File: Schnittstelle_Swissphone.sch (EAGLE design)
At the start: 22 parts, among them IC1 FT232RL, IC2 LM317LD

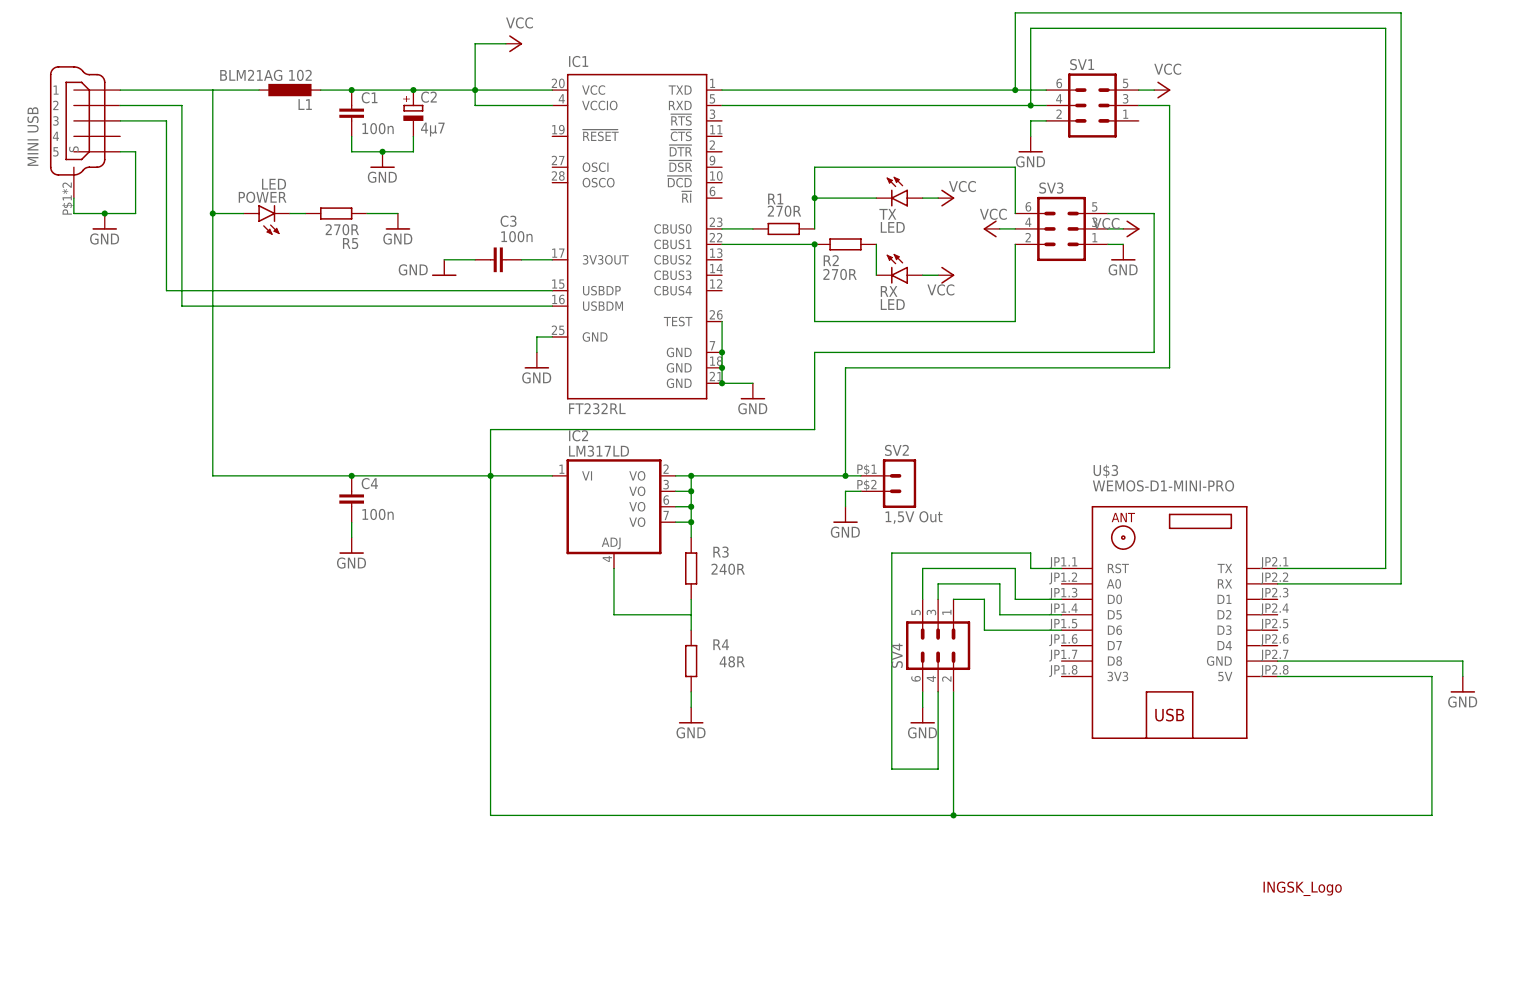
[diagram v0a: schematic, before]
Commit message: add Arduino Nano and ENC28J60
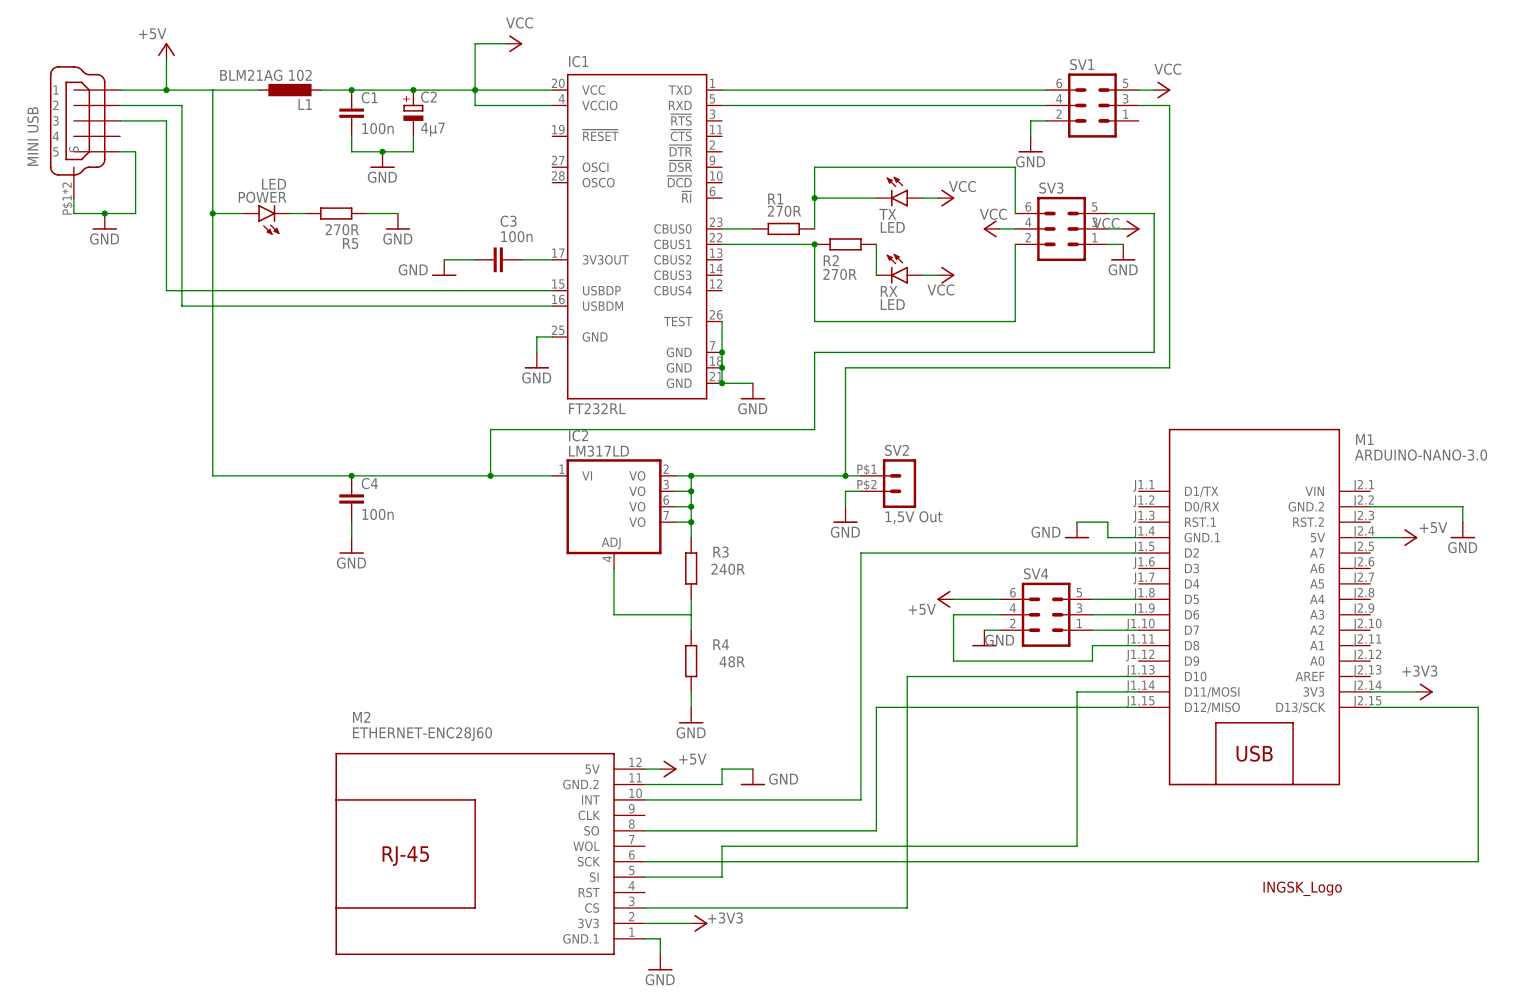
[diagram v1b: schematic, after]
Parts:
- removed U$3: WEMOS-D1-MINI-PRO, diy-modules:WEMOS-D1-MINI-PRO
- added M1: ARDUINO-NANO-3.0, diy-modules:ARDUINO-NANO-3.0
- added M2: ETHERNET-ENC28J60, diy-modules:ETHERNET-ENC28J60
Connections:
- new net +3V3: M1.3V3, M2.3V3
- new net +5V: C4.1, IC2.VI, L1.1, M1.5V, M2.5V, POWER.A, SV3.5, SV4.6, U$1.1
- new net N$18: M1.D5, SV4.5
- new net N$19: M1.D6, SV4.3
- new net N$20: M1.D7, SV4.1
- new net N$21: M1.D8, SV4.4
- net GND: now also M1.GND.1, M1.GND.2, M2.GND.1, M2.GND.2, SV4.2; no longer SV4.6, U$3.GND
- net N$11: now also M1.D12/MISO, M2.SO; no longer C4.1, IC2.VI, L1.1, POWER.A, SV3.5, SV4.2, U$1.1, U$3.5V
- net N$15: now also M1.D13/SCK, M2.SCK; no longer SV4.3, U$3.D5
- net N$16: now also M1.D11/MOSI, M2.SI; no longer SV4.5, U$3.D0
- net N$17: now also M1.D10, M2.CS; no longer SV4.4, U$3.RST
- net N$5: no longer U$3.RX
- net N$6: no longer U$3.TX
- net N$8: now also M1.D2, M2.INT; no longer SV4.1, U$3.D6
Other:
- moved on the sheet: SV4

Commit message: Add Layout
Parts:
- added SJ1, SJ2: (no value), jumper:SJ
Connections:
- removed net N$5: IC1.TXD, SV1.6
- new net N$22: M1.D0/RX, SJ1.1
- new net N$23: IC1.CBUS1, R2.1
- new net N$24: IC1.TXD, SJ1.2, SV1.6
- net N$2: now also R2.2, RX.C; no longer IC1.CBUS1, R2.1
- net N$4: now also M1.D1/TX, SJ2.1; no longer R2.2, RX.C
- net N$6: now also SJ2.2
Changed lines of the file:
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@@
 <part name="GND16" library="supply1" library_urn="urn:adsk.eagle:library:371" deviceset="GND" device=""/>
 <part name="P+10" library="supply1" library_urn="urn:adsk.eagle:library:371" deviceset="+5V" device=""/>
+<part name="SJ1" library="jumper" library_urn="urn:adsk.eagle:library:252" deviceset="SJ" device="" package3d_urn="urn:adsk.eagle:package:15471/1"/>
+<part name="SJ2" library="jumper" library_urn="urn:adsk.eagle:library:252" deviceset="SJ" device="" package3d_urn="urn:adsk.eagle:package:15471/1"/>
 </parts>
 <sheets>
@@
 <attribute name="VALUE" x="160.02" y="66.04" size="1.778" layer="96"/>
 </instance>
+<instance part="SJ1" gate="1" x="215.9" y="142.24" smashed="yes" rot="R90">
+<attribute name="NAME" x="213.36" y="139.7" size="1.778" layer="95" rot="R90"/>
+<attribute name="VALUE" x="219.71" y="139.7" size="1.778" layer="96" rot="R90"/>
+</instance>
+<instance part="SJ2" gate="1" x="223.52" y="142.24" smashed="yes" rot="R90">
+<attribute name="NAME" x="220.98" y="139.7" size="1.778" layer="95" rot="R90"/>
+<attribute name="VALUE" x="227.33" y="139.7" size="1.778" layer="96" rot="R90"/>
+</instance>
 </instances>
 <busses>
@@
 <net name="N$2" class="0">
 <segment>
-<pinref part="IC1" gate="1" pin="CBUS1"/>
-<pinref part="R2" gate="G$1" pin="1"/>
-<wire x1="129.54" y1="127" x2="144.78" y2="127" width="0.1524" layer="91"/>
-<wire x1="144.78" y1="127" x2="144.78" y2="114.3" width="0.1524" layer="91"/>
-<wire x1="144.78" y1="114.3" x2="177.8" y2="114.3" width="0.1524" layer="91"/>
-<junction x="144.78" y="127"/>
 <pinref part="SV3" gate="1" pin="2"/>
 <wire x1="177.8" y1="114.3" x2="177.8" y2="127" width="0.1524" layer="91"/>
-</segment>
-</net>
-<net name="N$4" class="0">
-<segment>
 <pinref part="R2" gate="G$1" pin="2"/>
 <wire x1="154.94" y1="127" x2="154.94" y2="121.92" width="0.1524" layer="91"/>
 <pinref part="RX" gate="G$1" pin="C"/>
+<wire x1="177.8" y1="114.3" x2="154.94" y2="114.3" width="0.1524" layer="91"/>
+<wire x1="154.94" y1="114.3" x2="154.94" y2="121.92" width="0.1524" layer="91"/>
+<junction x="154.94" y="121.92"/>
 </segment>
 </net>
 <net name="N$3" class="0">
 <segment>
+<pinref part="SV3" gate="1" pin="6"/>
+<wire x1="177.8" y1="139.7" x2="177.8" y2="132.08" width="0.1524" layer="91"/>
+<wire x1="177.8" y1="139.7" x2="154.94" y2="139.7" width="0.1524" layer="91"/>
+<pinref part="TX" gate="G$1" pin="C"/>
+<wire x1="144.78" y1="134.62" x2="154.94" y2="134.62" width="0.1524" layer="91"/>
 <pinref part="R1" gate="G$1" pin="2"/>
 <wire x1="144.78" y1="129.54" x2="144.78" y2="134.62" width="0.1524" layer="91"/>
-<pinref part="TX" gate="G$1" pin="C"/>
-<wire x1="144.78" y1="134.62" x2="154.94" y2="134.62" width="0.1524" layer="91"/>
-<wire x1="144.78" y1="134.62" x2="144.78" y2="139.7" width="0.1524" layer="91"/>
-<wire x1="144.78" y1="139.7" x2="177.8" y2="139.7" width="0.1524" layer="91"/>
-<junction x="144.78" y="134.62"/>
-<pinref part="SV3" gate="1" pin="6"/>
-<wire x1="177.8" y1="139.7" x2="177.8" y2="132.08" width="0.1524" layer="91"/>
+<wire x1="154.94" y1="139.7" x2="154.94" y2="134.62" width="0.1524" layer="91"/>
+<junction x="154.94" y="134.62"/>
 </segment>
 </net>
@@
 </segment>
 </net>
-<net name="N$5" class="0">
-<segment>
-<pinref part="IC1" gate="1" pin="TXD"/>
-<wire x1="129.54" y1="152.4" x2="182.88" y2="152.4" width="0.1524" layer="91"/>
-<pinref part="SV1" gate="1" pin="6"/>
-</segment>
-</net>
 <net name="N$6" class="0">
 <segment>
 <pinref part="IC1" gate="1" pin="RXD"/>
 <pinref part="SV1" gate="1" pin="4"/>
-<wire x1="182.88" y1="149.86" x2="129.54" y2="149.86" width="0.1524" layer="91"/>
+<wire x1="182.88" y1="149.86" x2="177.8" y2="149.86" width="0.1524" layer="91"/>
+<pinref part="SJ2" gate="1" pin="2"/>
+<wire x1="177.8" y1="149.86" x2="129.54" y2="149.86" width="0.1524" layer="91"/>
+<wire x1="223.52" y1="147.32" x2="223.52" y2="165.1" width="0.1524" layer="91"/>
+<wire x1="223.52" y1="165.1" x2="177.8" y2="165.1" width="0.1524" layer="91"/>
+<wire x1="177.8" y1="165.1" x2="177.8" y2="149.86" width="0.1524" layer="91"/>
+<junction x="177.8" y="149.86"/>
 </segment>
 </net>
@@
 </segment>
 </net>
+<net name="N$23" class="0">
+<segment>
+<pinref part="R2" gate="G$1" pin="1"/>
+<pinref part="IC1" gate="1" pin="CBUS1"/>
+<wire x1="129.54" y1="127" x2="144.78" y2="127" width="0.1524" layer="91"/>
+</segment>
+</net>
+<net name="N$4" class="0">
+<segment>
+<pinref part="M1" gate="G$1" pin="D1/TX"/>
+<wire x1="198.12" y1="86.36" x2="195.58" y2="86.36" width="0.1524" layer="91"/>
+<wire x1="195.58" y1="86.36" x2="195.58" y2="99.06" width="0.1524" layer="91"/>
+<pinref part="SJ2" gate="1" pin="1"/>
+<wire x1="223.52" y1="137.16" x2="223.52" y2="99.06" width="0.1524" layer="91"/>
+<wire x1="223.52" y1="99.06" x2="195.58" y2="99.06" width="0.1524" layer="91"/>
+</segment>
+</net>
+<net name="N$22" class="0">
+<segment>
+<pinref part="M1" gate="G$1" pin="D0/RX"/>
+<wire x1="198.12" y1="83.82" x2="193.04" y2="83.82" width="0.1524" layer="91"/>
+<wire x1="193.04" y1="83.82" x2="193.04" y2="101.6" width="0.1524" layer="91"/>
+<wire x1="193.04" y1="101.6" x2="215.9" y2="101.6" width="0.1524" layer="91"/>
+<pinref part="SJ1" gate="1" pin="1"/>
+<wire x1="215.9" y1="101.6" x2="215.9" y2="137.16" width="0.1524" layer="91"/>
+</segment>
+</net>
+<net name="N$24" class="0">
+<segment>
+<pinref part="SJ1" gate="1" pin="2"/>
+<wire x1="215.9" y1="147.32" x2="215.9" y2="162.56" width="0.1524" layer="91"/>
+<pinref part="IC1" gate="1" pin="TXD"/>
+<wire x1="129.54" y1="152.4" x2="180.34" y2="152.4" width="0.1524" layer="91"/>
+<pinref part="SV1" gate="1" pin="6"/>
+<wire x1="180.34" y1="152.4" x2="182.88" y2="152.4" width="0.1524" layer="91"/>
+<wire x1="215.9" y1="162.56" x2="180.34" y2="162.56" width="0.1524" layer="91"/>
+<wire x1="180.34" y1="162.56" x2="180.34" y2="152.4" width="0.1524" layer="91"/>
+<junction x="180.34" y="152.4"/>
+</segment>
+</net>

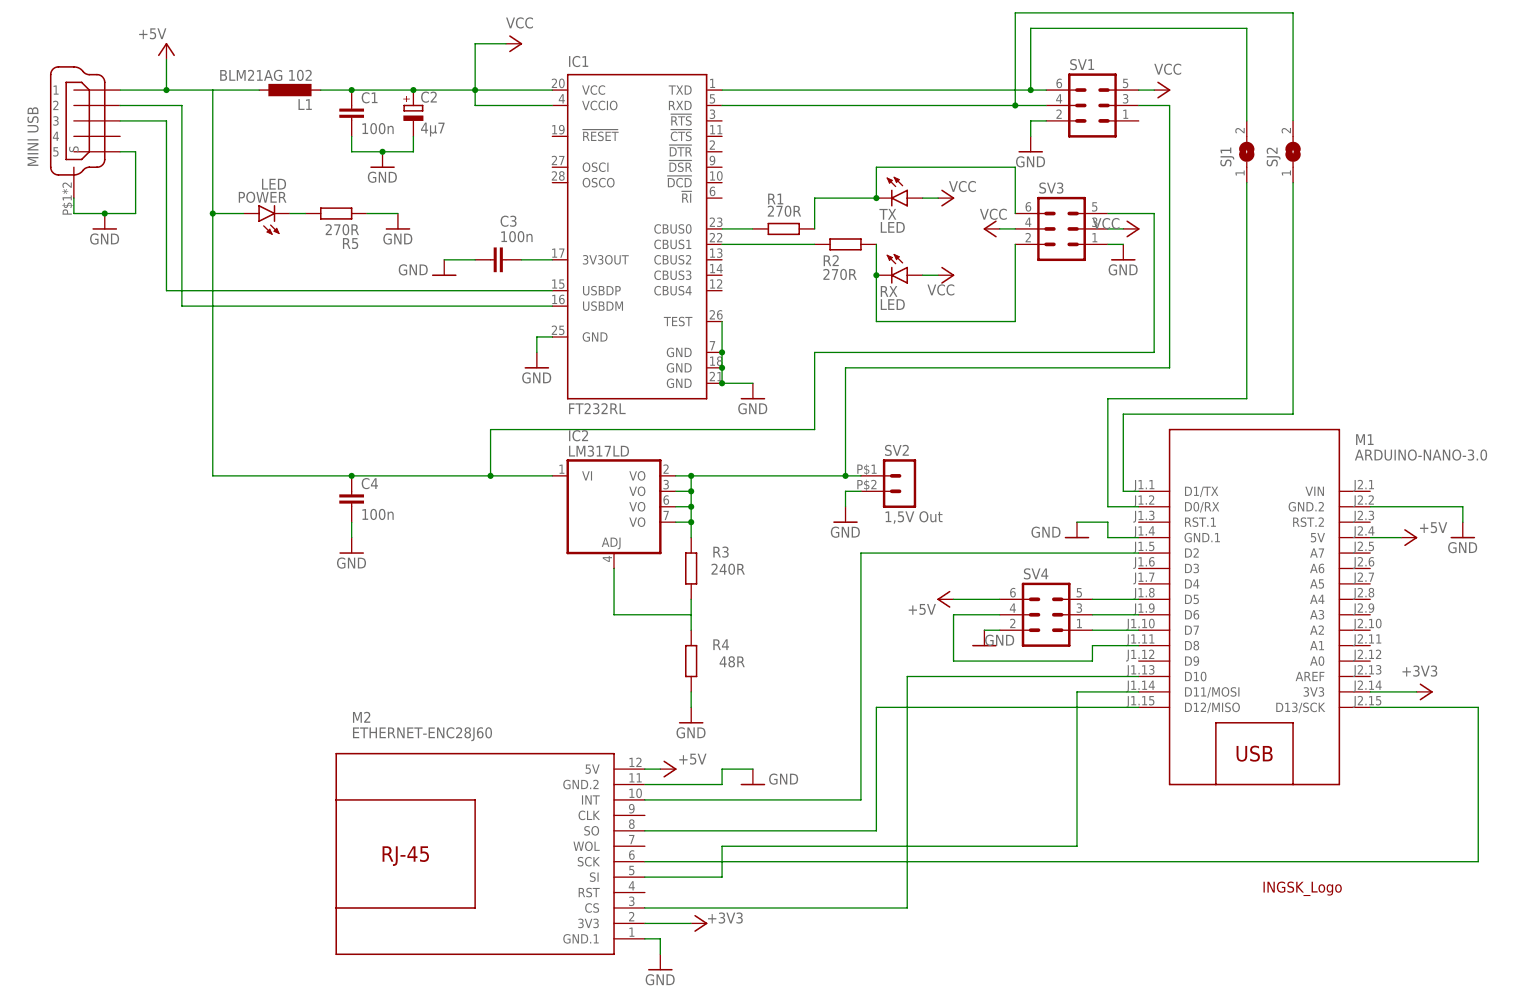
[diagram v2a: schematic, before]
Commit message: PCB wo. Ethernet
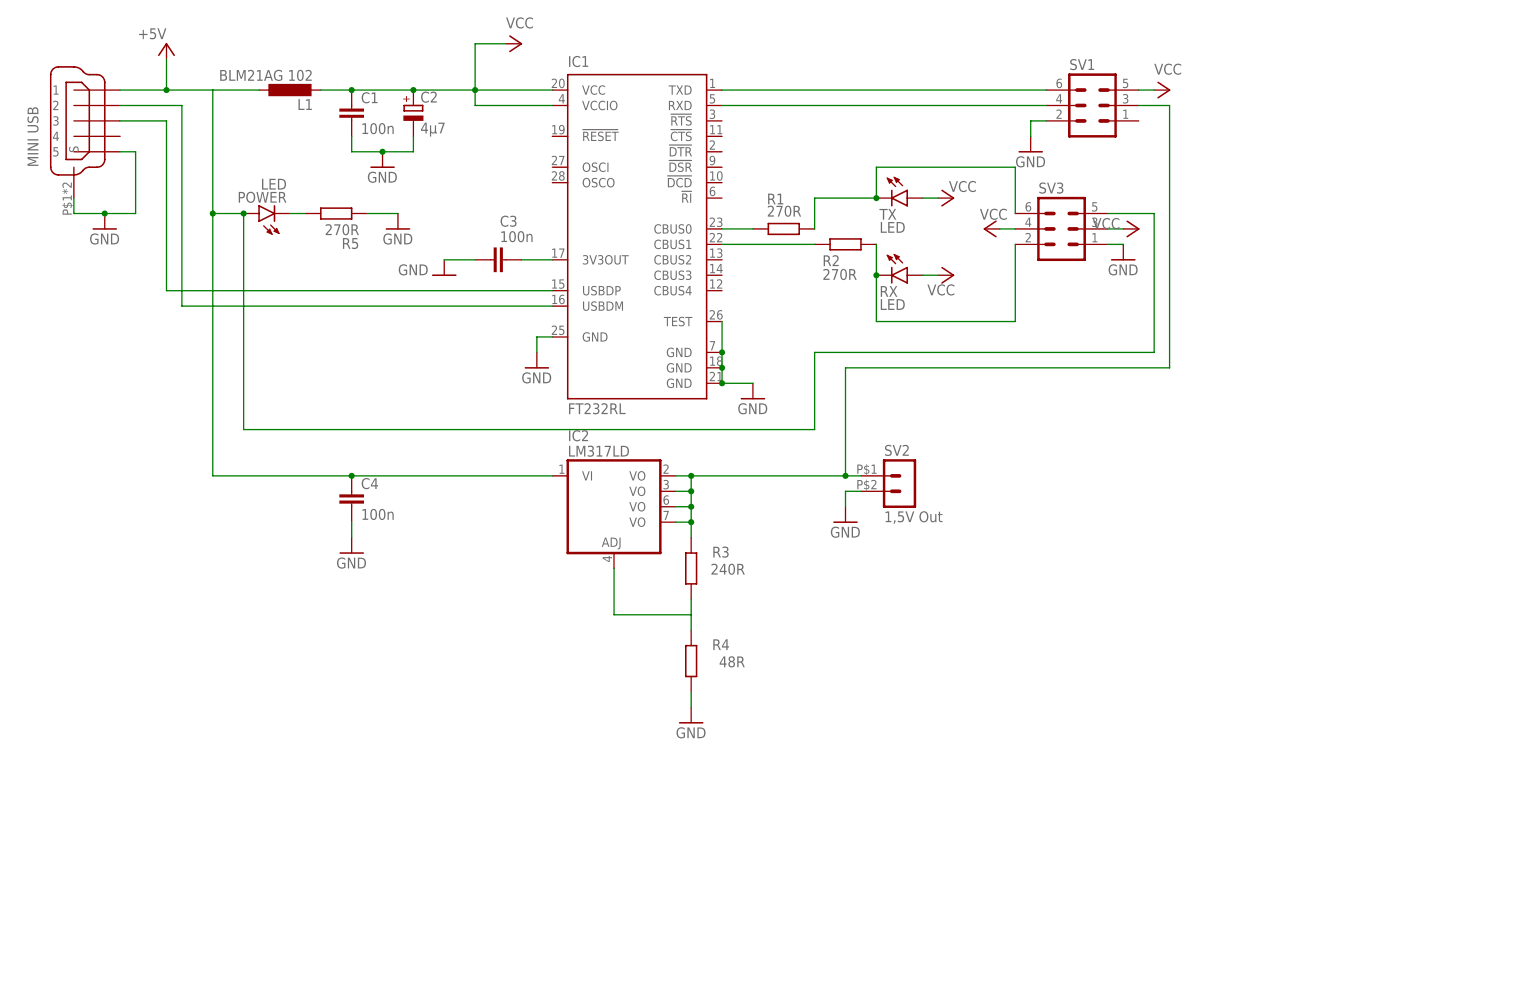
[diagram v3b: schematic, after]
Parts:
- removed M1: ARDUINO-NANO-3.0, diy-modules:ARDUINO-NANO-3.0
- removed M2: ETHERNET-ENC28J60, diy-modules:ETHERNET-ENC28J60
- removed SJ1, SJ2: (no value), jumper:SJ
- removed SV4: (no value), con-harting-ml:ML6
- removed U$2: SK, EigeneLogos:SK
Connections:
- removed net +3V3: M1.3V3, M2.3V3
- removed net N$11: M1.D12/MISO, M2.SO
- removed net N$15: M1.D13/SCK, M2.SCK
- removed net N$16: M1.D11/MOSI, M2.SI
- removed net N$17: M1.D10, M2.CS
- removed net N$18: M1.D5, SV4.5
- removed net N$19: M1.D6, SV4.3
- removed net N$20: M1.D7, SV4.1
- removed net N$21: M1.D8, SV4.4
- removed net N$22: M1.D0/RX, SJ1.1
- removed net N$4: M1.D1/TX, SJ2.1
- removed net N$8: M1.D2, M2.INT
- net +5V: no longer M1.5V, M2.5V, SV4.6
- net GND: no longer M1.GND.1, M1.GND.2, M2.GND.1, M2.GND.2, SV4.2
- net N$24: no longer SJ1.2
- net N$6: no longer SJ2.2
